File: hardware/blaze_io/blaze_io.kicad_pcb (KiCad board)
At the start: 2 copper layers, 70 x 70 mm, 2 parts, among them J2 Conn_01x30_Pin, J3 Conn_01x30_Socket

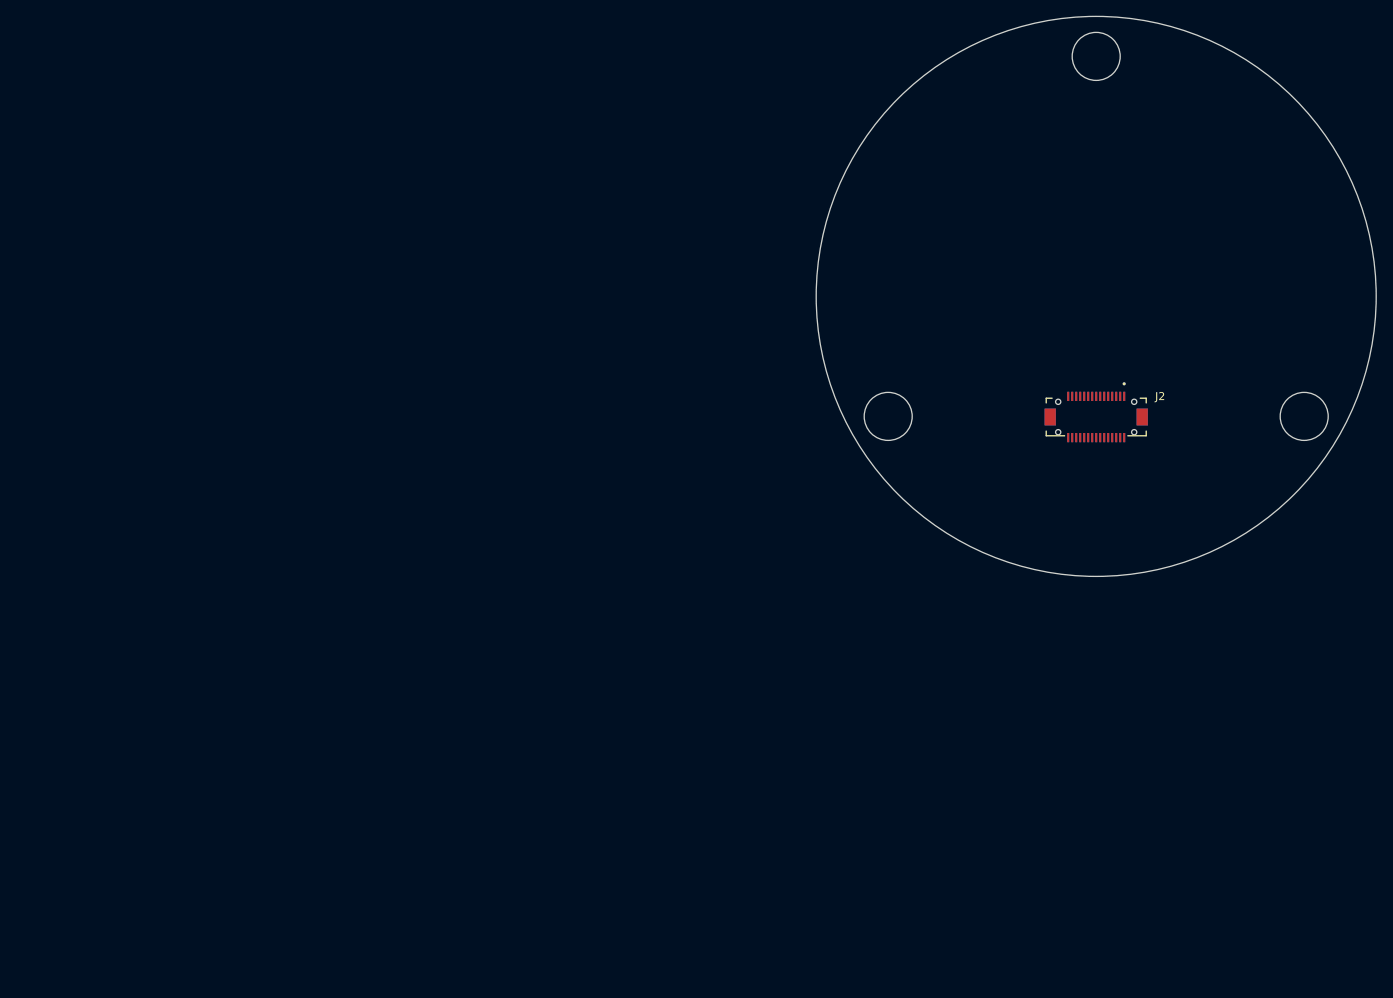
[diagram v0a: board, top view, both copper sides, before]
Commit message: Component grouping
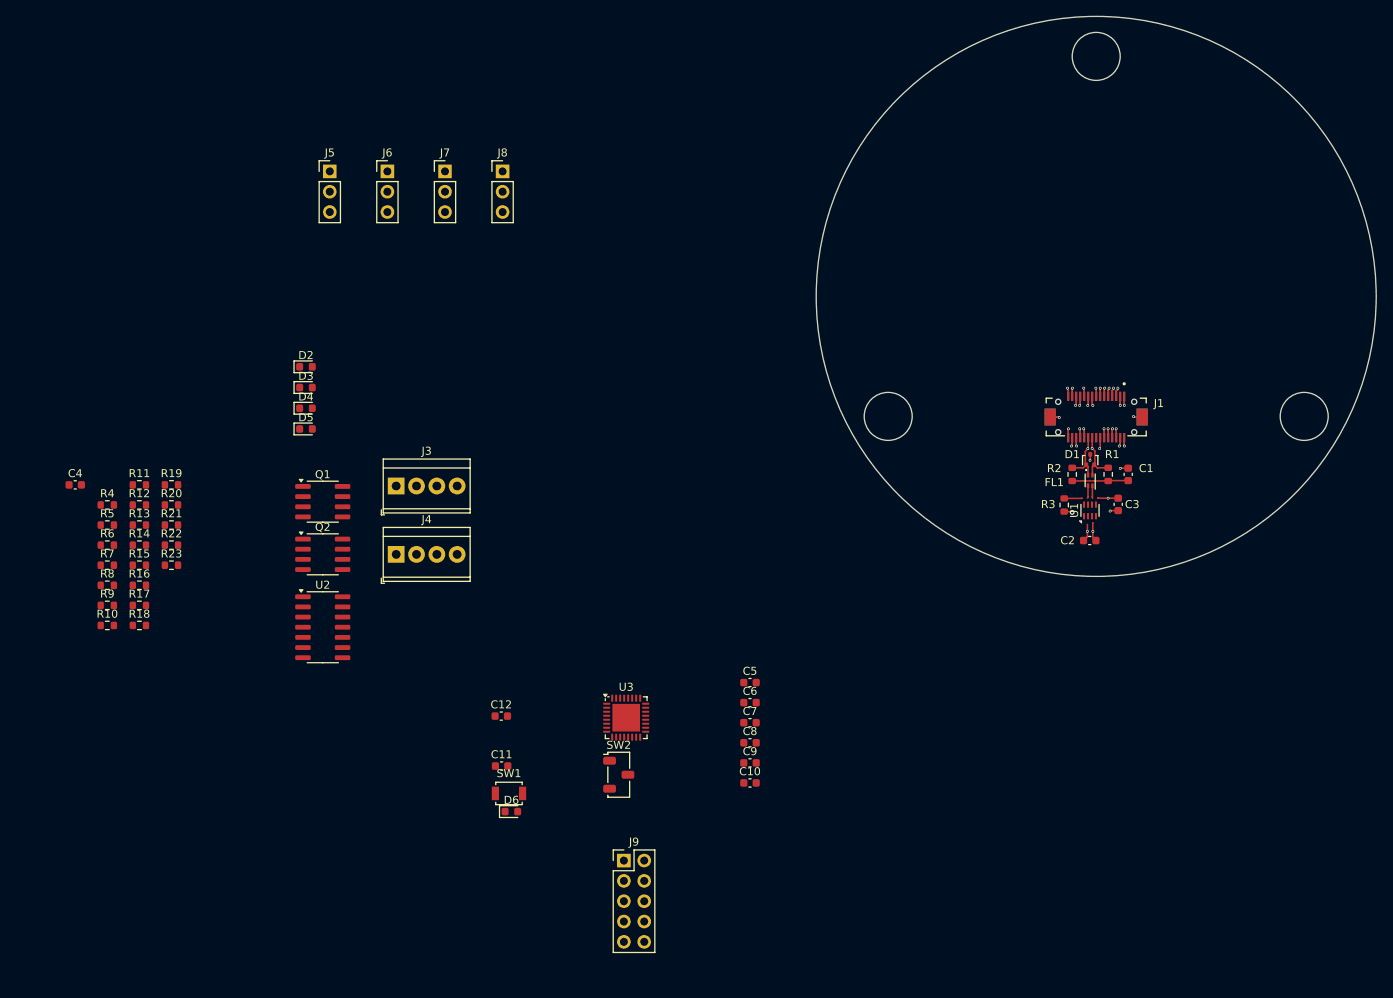
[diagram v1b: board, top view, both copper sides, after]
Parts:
- added C1: 4.7nF, Capacitor_SMD:C_0603_1608Metric, F.Cu at (152.5, 127.8)
- added C10: 0.1uF, Capacitor_SMD:C_0603_1608Metric, F.Cu at (105.2, 166.3)
- added C11: 0.1uF, Capacitor_SMD:C_0603_1608Metric, F.Cu at (74.2, 164.2)
- added C12: 2.2uF, Capacitor_SMD:C_0603_1608Metric, F.Cu at (74.1, 158.0)
- added C2: 0.1uF, Capacitor_SMD:C_0603_1608Metric, F.Cu at (147.7, 136.0)
- added C3: 0.1uF, Capacitor_SMD:C_0603_1608Metric, F.Cu at (151.2, 131.5)
- added C4: 0.1uF, Capacitor_SMD:C_0603_1608Metric, F.Cu at (20.9, 129.1)
- added C5: 2.2uF, Capacitor_SMD:C_0603_1608Metric, F.Cu at (105.2, 153.8)
- added C6: 0.1uF, Capacitor_SMD:C_0603_1608Metric, F.Cu at (105.2, 156.3)
- added C7: 4.7uF, Capacitor_SMD:C_0603_1608Metric, F.Cu at (105.2, 158.8)
- added C8: 0.1uF, Capacitor_SMD:C_0603_1608Metric, F.Cu at (105.2, 161.3)
- added C9: 1uF, Capacitor_SMD:C_0603_1608Metric, F.Cu at (105.2, 163.8)
- added D1: ESDCAN03-2BM3Y, Package_TO_SOT_SMD:SOT-416, F.Cu at (147.8, 125.9)
- added D2: LED, LED_SMD:LED_0603_1608Metric, F.Cu at (49.7, 114.3)
- added D3: LED, LED_SMD:LED_0603_1608Metric, F.Cu at (49.7, 116.9)
- added D4: LED, LED_SMD:LED_0603_1608Metric, F.Cu at (49.7, 119.5)
- added D5: LED, LED_SMD:LED_0603_1608Metric, F.Cu at (49.7, 122.1)
- added D6: D_Schottky, Diode_SMD:D_0603_1608Metric, F.Cu at (75.4, 169.9)
- added FL1: Choke, Inductor_SMD:L_CommonModeChoke_Coilcraft_0603USB, F.Cu at (147.8, 128.5)
- added J3: Conn_01x04, TerminalBlock_TE-Connectivity:TerminalBlock_TE_282834-4_1x04_P2.54mm_Horizontal, F.Cu at (61.0, 129.2)
- added J4: Conn_01x04, TerminalBlock_TE-Connectivity:TerminalBlock_TE_282834-4_1x04_P2.54mm_Horizontal, F.Cu at (61.0, 137.8)
- added J5: Conn_01x03_Pin, Connector_PinHeader_2.54mm:PinHeader_1x03_P2.54mm_Vertical, F.Cu at (52.7, 89.9)
- added J6: Conn_01x03_Pin, Connector_PinHeader_2.54mm:PinHeader_1x03_P2.54mm_Vertical, F.Cu at (59.9, 89.9)
- added J7: Conn_01x03_Pin, Connector_PinHeader_2.54mm:PinHeader_1x03_P2.54mm_Vertical, F.Cu at (67.1, 89.9)
- added J8: Conn_01x03_Pin, Connector_PinHeader_2.54mm:PinHeader_1x03_P2.54mm_Vertical, F.Cu at (74.3, 89.9)
- added J9: JTAG, Connector_PinHeader_2.54mm:PinHeader_2x05_P2.54mm_Vertical, F.Cu at (89.5, 176.0)
- added Q1: AO4892, Package_SO:SOIC-8_3.9x4.9mm_P1.27mm, F.Cu at (51.8, 131.2)
- added Q2: AO4892, Package_SO:SOIC-8_3.9x4.9mm_P1.27mm, F.Cu at (51.8, 137.7)
- added R1: 60, Resistor_SMD:R_0603_1608Metric, F.Cu at (150.0, 127.8)
- added R10: 10K, Resistor_SMD:R_0603_1608Metric, F.Cu at (24.9, 146.6)
- added R11: 10K, Resistor_SMD:R_0603_1608Metric, F.Cu at (28.9, 129.1)
- added R12: R_US, Resistor_SMD:R_0603_1608Metric, F.Cu at (28.9, 131.6)
- added R13: R_US, Resistor_SMD:R_0603_1608Metric, F.Cu at (28.9, 134.1)
- added R14: 100K, Resistor_SMD:R_0603_1608Metric, F.Cu at (28.9, 136.6)
- added R15: 100K, Resistor_SMD:R_0603_1608Metric, F.Cu at (28.9, 139.1)
- added R16: R_US, Resistor_SMD:R_0603_1608Metric, F.Cu at (28.9, 141.6)
- added R17: R_US, Resistor_SMD:R_0603_1608Metric, F.Cu at (28.9, 144.1)
- added R18: 100, Resistor_SMD:R_0603_1608Metric, F.Cu at (28.9, 146.6)
- added R19: 100, Resistor_SMD:R_0603_1608Metric, F.Cu at (32.9, 129.1)
- added R2: 60, Resistor_SMD:R_0603_1608Metric, F.Cu at (145.5, 127.8)
- added R20: 10K, Resistor_SMD:R_0603_1608Metric, F.Cu at (32.9, 131.6)
- added R21: 10K, Resistor_SMD:R_0603_1608Metric, F.Cu at (32.9, 134.1)
- added R22: R_US, Resistor_SMD:R_0603_1608Metric, F.Cu at (32.9, 136.6)
- added R23: R_US, Resistor_SMD:R_0603_1608Metric, F.Cu at (32.9, 139.1)
- added R3: 10K, Resistor_SMD:R_0603_1608Metric, F.Cu at (144.5, 131.6)
- added R4: 100K, Resistor_SMD:R_0603_1608Metric, F.Cu at (24.9, 131.6)
- added R5: 100K, Resistor_SMD:R_0603_1608Metric, F.Cu at (24.9, 134.1)
- added R6: R_US, Resistor_SMD:R_0603_1608Metric, F.Cu at (24.9, 136.6)
- added R7: R_US, Resistor_SMD:R_0603_1608Metric, F.Cu at (24.9, 139.1)
- added R8: 100, Resistor_SMD:R_0603_1608Metric, F.Cu at (24.9, 141.6)
- added R9: 100, Resistor_SMD:R_0603_1608Metric, F.Cu at (24.9, 144.1)
- added SW1: SW_SPST, Button_Switch_SMD:SW_SPST_B3U-1000P, F.Cu at (75.1, 167.6)
- added SW2: SW_SPDT, Button_Switch_SMD:Nidec_Copal_CAS-120A, F.Cu at (88.8, 165.3)
- added U1: TCAN1044VDDFR, Package_SON:Texas_VSON-HR-8_1.5x2mm_P0.5mm, F.Cu at (147.7, 132.2)
- added U2: 4081, Package_SO:SOIC-14_3.9x8.7mm_P1.27mm, F.Cu at (51.8, 146.9)
- added U3: STM32H503KBUx, Package_DFN_QFN:QFN-32-1EP_5x5mm_P0.5mm_EP3.45x3.45mm, F.Cu at (89.8, 158.2)
- renumbered J2 to J1, J3 to J2
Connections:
- net /RX_RADIO renamed Net-(J1-Pin_6)
- net /TX_RADIO renamed Net-(J1-Pin_5)
- J1 pad 1: Net-(J2-Pin_1) -> VBATT
- J1 pad 2: Net-(J2-Pin_2) -> VBATT
- J2 pad 29: Net-(J2-Pin_2) -> VBATT
- J2 pad 30: Net-(J2-Pin_1) -> VBATT
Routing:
- net +5V: track 0.00 -> 33.1 mm, vias 0 -> 7
- net GND: track 0.00 -> 18.2 mm, vias 0 -> 10
- net +3V3: track 0.00 -> 12.4 mm, vias 0 -> 6
- net /CANH: track 0.00 -> 8.34 mm, vias 0 -> 2
- net Net-(C1-Pad1): track 0.00 -> 7.28 mm
- net /CANL: track 0.00 -> 6.90 mm, vias 0 -> 1
- net VBATT: track 0.00 -> 4.53 mm, vias 0 -> 2
- net /PPS: track 0.00 -> 2.33 mm, vias 0 -> 1
- net Net-(J1-Pin_10): track 0.00 -> 2.30 mm, vias 0 -> 1
- net /CAN_STB: track 0.00 -> 2.27 mm
- net Net-(J1-Pin_19): track 0.00 -> 2.26 mm, vias 0 -> 1
- net Net-(J1-Pin_20): track 0.00 -> 2.26 mm, vias 0 -> 1
- net Net-(J1-Pin_16): track 0.00 -> 2.23 mm, vias 0 -> 1
- net Net-(J1-Pin_17): track 0.00 -> 2.18 mm, vias 0 -> 1
- net Net-(J1-Pin_5): track 0.00 -> 2.16 mm, vias 0 -> 1
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- added copper zone on In1.Cu, net +3V3
- added copper zone on In2.Cu, net GND
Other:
- copper layers 2 -> 4
